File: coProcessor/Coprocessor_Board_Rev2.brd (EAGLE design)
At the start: 101.6 x 101.6 mm, 85 parts, among them IC1 STM32F405RGT6, J1 USB_MINI-B_SMT, J4 30320-6002HB, J5 5008730806, P1 39-30-08?, Q1 L78M05CV, U1 MCP2561-E/P

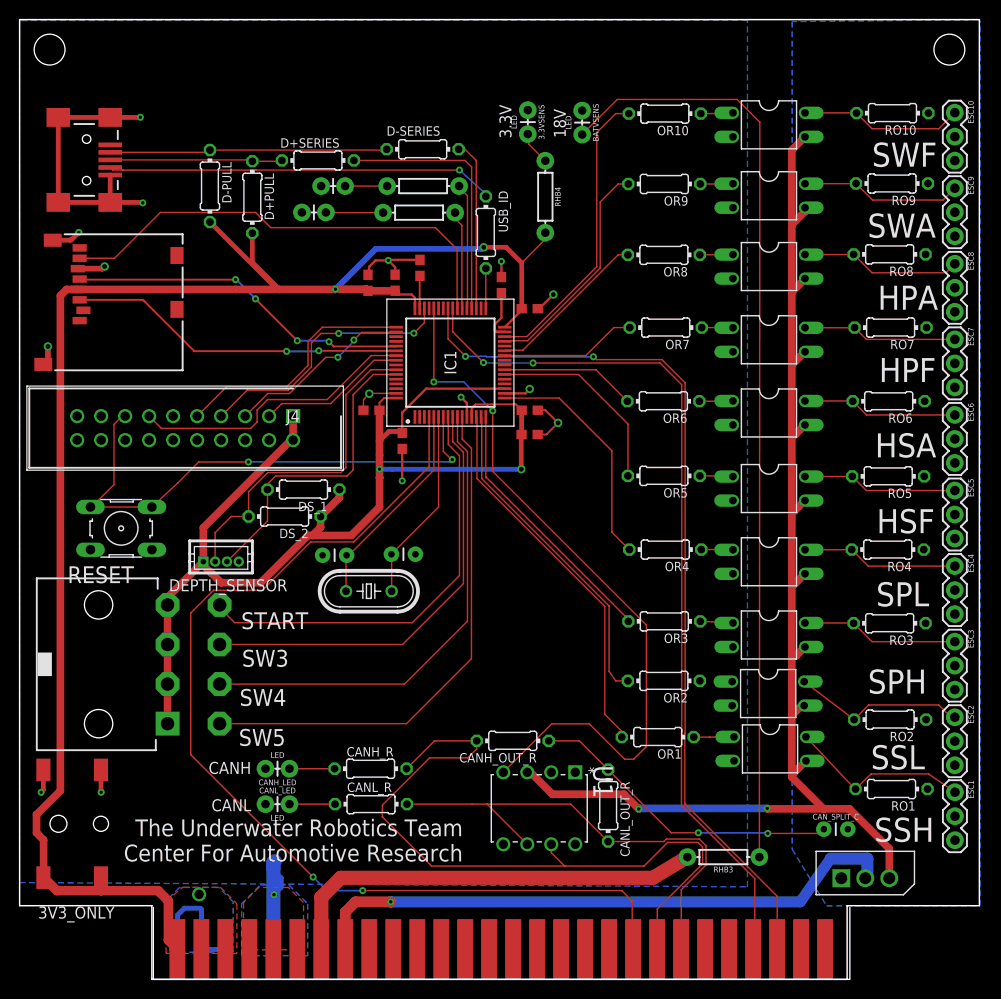
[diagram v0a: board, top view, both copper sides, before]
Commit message: replaced 5v can tran with correct 3.3v
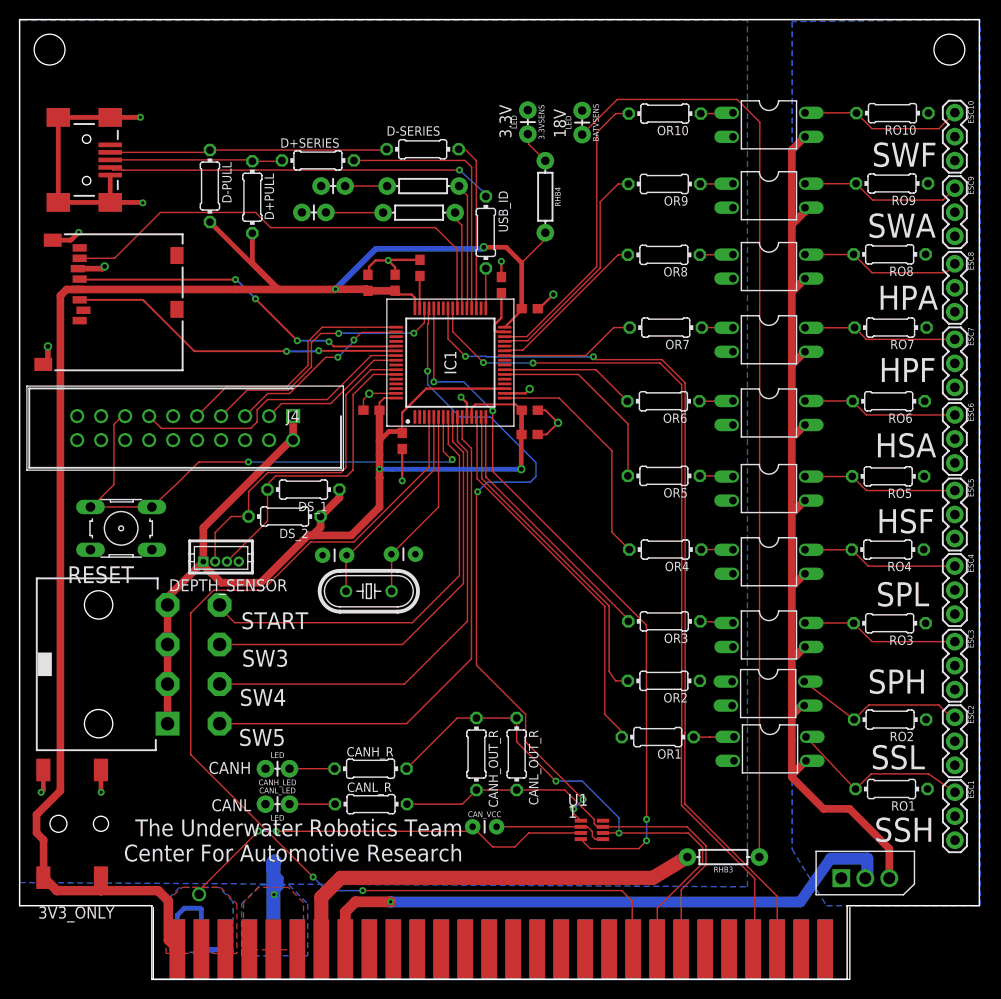
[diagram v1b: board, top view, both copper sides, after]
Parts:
- removed CAN_SPLIT_C: 4700 pF, SparkFun-Capacitors:CAP-PTH-2.54
- added CAN_VCC: .1 uF, SparkFun-Capacitors:CAP-PTH-2.54
- CANH_OUT_R, CANL_OUT_R: value 60 -> 120
- U1: value MCP2561-E/P -> MAX3051ESA; device Microchip-MCP2561-E_P:DIP254P762X533-8 -> MAX3051ESA:8-SOICN
- moved CANL_OUT_R 11.1 mm to (52.6, 23.9)
- moved U1 9.50 mm to (60.6, 15.8), turned to 0 degrees
- moved CANH_OUT_R 4.09 mm to (48.4, 23.9), turned to 270 degrees
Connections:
- removed net SPLIT: CANH_OUT_R.1, CANL_OUT_R.1, CAN_SPLIT_C.1
- removed net VSS: U1.2
- net 3.3V: now also CAN_VCC.1, U1.3
- net 5V: no longer U1.3
- net CAN1_TXD: now also U1.1
- net CANH: now also CANH_OUT_R.1, CANL_OUT_R.1; no longer CANH_OUT_R.2
- net CANL: now also CANH_OUT_R.2
- net GND: now also CANH_LED.P$2, CANL_LED.P$1, CAN_VCC.2, U1.2, U1.8
- net GNDBAT: no longer CANH_LED.P$2, CANL_LED.P$1, CAN_SPLIT_C.2
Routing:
- net CAN1_TXD: track 0.00 -> 71.6 mm, vias 0 -> 4
- net 3.3V: track 314.2 -> 359.4 mm, vias 5 -> 7
- net SPLIT: track 33.4 -> 0.00 mm, vias 2 -> 0
- net 5V: track 135.5 -> 102.5 mm, vias 2 -> 0
- net CANH: track 76.3 -> 56.1 mm, vias 0 -> 2
- net GND: track 88.7 -> 100.8 mm
- net CANL: track 51.8 -> 47.0 mm
- net CAN1_RXD: track 77.0 -> 75.3 mm, vias 2 -> 4

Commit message: 2 pin connector for can. please check... USB moved No usb id line Different switch connector, custom-made 12 pin package Esc names horizontal LEDs for programming Pushbutton for programming 4 leds , 1 pushbutton
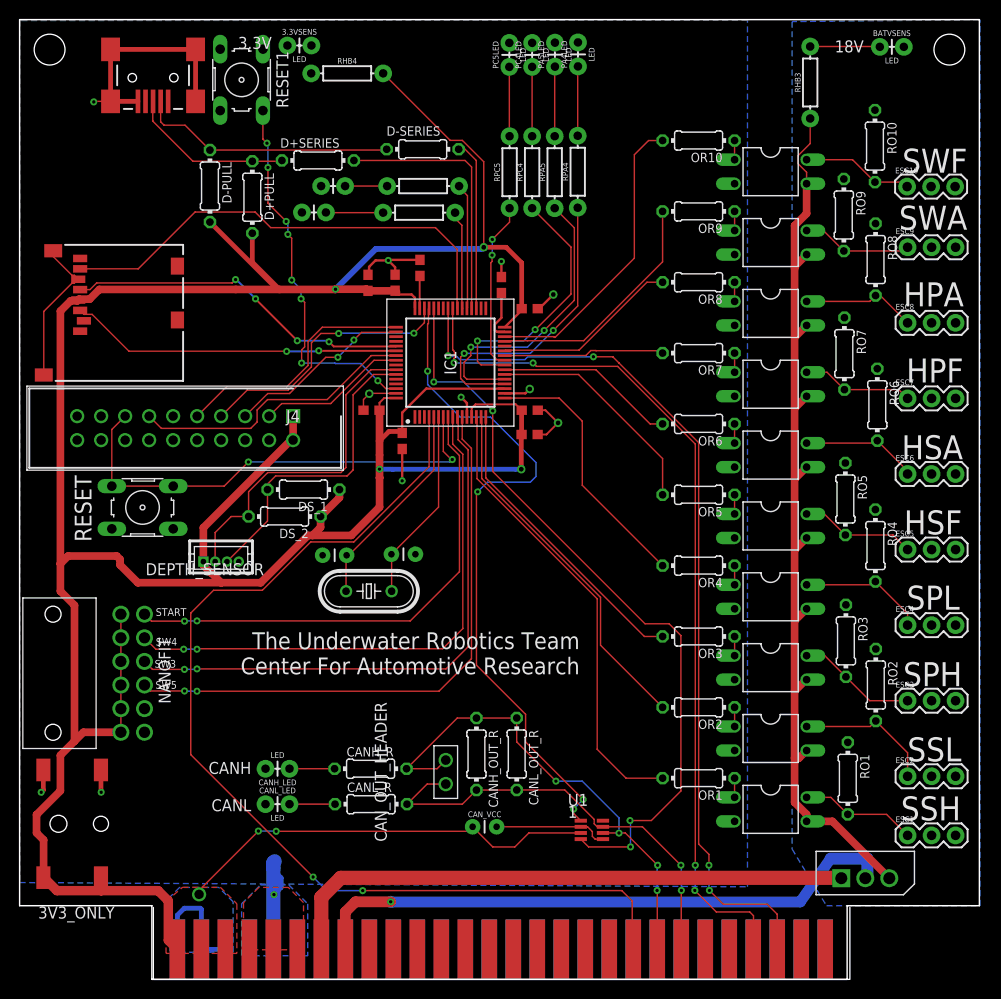
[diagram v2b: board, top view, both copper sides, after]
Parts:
- removed P1: 39-30-08?, con-molex-mini-fit:39-30-?08?
- removed USB_ID: 0Ω, resistor:0204/7
- added CAN_OUT_HEADER: (no value), Wurth_Elektronik_Electromechanic_Board_to_Board_Connectors_rev16a:61300211821
- added PA4LED, PA5LED, PC4LED, PC5LED: LED, SparkFun-Resistors:AXIAL-0.1
- added RESET1: (no value), switch-omron:B3F-10XX
- added RPA4, RPA5, RPC4, RPC5: 1k, SparkFun-Resistors:AXIAL-0.3
- added U$2: 105314-2112, 105314-2112 nanofit hdr:105314-2112
- RHB3: value 7k -> 1.5k
- moved RHB3 82.5 mm to (83.7, 94.9), turned to 90 degrees
- moved BATVSENS 33.7 mm to (92.3, 98.7), turned to 0 degrees
- moved 3.3VSENS 25.5 mm to (29.6, 98.9), turned to 0 degrees
- moved RHB4 24.7 mm to (34.7, 95.9), turned to 0 degrees
- moved J1 11.2 mm to (14.1, 95.4), turned to 270 degrees
- moved ESC10 9.31 mm to (93.9, 83.9), turned to 0 degrees
- moved ESC2 8.00 mm to (94.0, 21.5), turned to 0 degrees
- moved ESC3 8.00 mm to (94.0, 29.5), turned to 0 degrees
- moved ESC4 8.00 mm to (94.0, 37.5), turned to 0 degrees
- moved ESC5 8.00 mm to (94.0, 45.5), turned to 0 degrees
- moved ESC6 8.00 mm to (94.0, 53.5), turned to 0 degrees
- moved ESC7 8.00 mm to (94.0, 61.5), turned to 0 degrees
- moved ESC8 8.00 mm to (94.0, 69.5), turned to 0 degrees
- moved ESC9 8.00 mm to (94.0, 77.5), turned to 0 degrees
- moved ESC1 6.78 mm to (94.0, 15.2), turned to 0 degrees
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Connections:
- removed net OTG_ID: IC1.33, USB_ID.1
- removed net OTG_ID_CON: J1.ID, USB_ID.2
- new net GNDA: BATVSENS.P$2
- new net HEARTBEAT_3: IC1.20, RPA4.P$1
- new net HEARTBEAT_4: IC1.21, RPA5.P$1
- new net N$10: PC4LED.P$1, RPC4.P$2
- new net N$11: PC5LED.P$1, RPC5.P$2
- new net N$12: IC1.62, RESET1.2
- new net N$7: PA4LED.P$1, RPA4.P$2
- new net N$8: PA5LED.P$1, RPA5.P$2
- new net N$9: RESET1.3, RESET1.4
- new net PC4: IC1.24, RPC4.P$1
- new net PC5: IC1.25, RPC5.P$1
- net 18V: now also Q1.1; no longer RHB3.P$2
- net 3.3V: now also U$2.CK10, U$2.CK11, U$2.CK12, U$2.CK7, U$2.CK8, U$2.CK9; no longer P1.1, P1.2, P1.3, P1.4
- net 5V: now also RHB3.P$1
- net CANH: now also CAN_OUT_HEADER.2
- net CANL: now also CAN_OUT_HEADER.1
- net GND: now also PA4LED.P$2, PA5LED.P$2, PC4LED.P$2, PC5LED.P$2
- net GNDBAT: no longer BATVSENS.P$1, Q1.1
- net MISSION_START: now also U$2.CK6; no longer P1.8
- net N$3: now also BATVSENS.P$1, RHB3.P$2; no longer BATVSENS.P$2, RHB3.P$1
- net SWITCH_3: now also U$2.CK5; no longer P1.7
- net SWITCH_4: now also U$2.CK4; no longer P1.6
- net SWITCH_5: now also U$2.CK3; no longer P1.5
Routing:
- net N$3: track 99.1 -> 7.39 mm
- net OTG_ID_CON: track 41.1 -> 0.00 mm, vias 1 -> 0
- net N$12: track 0.00 -> 39.8 mm, vias 0 -> 8
- net 3.3V: track 359.4 -> 396.9 mm
- net HEARTBEAT_3: track 0.00 -> 32.2 mm, vias 0 -> 2
- net HEARTBEAT_4: track 0.00 -> 31.4 mm, vias 0 -> 2
- net PC4: track 0.00 -> 28.0 mm, vias 0 -> 2
- net PC5: track 0.00 -> 18.0 mm, vias 0 -> 2
- net 18V: track 45.7 -> 61.4 mm
- net SWITCH_3: track 46.6 -> 57.9 mm, vias 0 -> 2
- net SWITCH_4: track 51.0 -> 60.4 mm, vias 0 -> 2
- net SURGESTBDHI: track 40.3 -> 48.7 mm
- net N$8: track 0.00 -> 7.38 mm
- net N$7: track 0.00 -> 7.35 mm
- net N$11: track 0.00 -> 7.35 mm
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
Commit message: added gpio pin connector, erc, fixed some air wires
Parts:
- removed CAN_OUT_HEADER: (no value), Wurth_Elektronik_Electromechanic_Board_to_Board_Connectors_rev16a:61300211821
- added GPIO: (no value), SparkFun-Connectors:1X03
- added J2: (no value), SparkFun-Connectors:1X02
- renumbered RESET1 to DEBUG
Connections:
- removed net N$2: 3.3VSENS.P$1
- new net PB8: GPIO.3, IC1.61
- new net PC13: GPIO.2, IC1.2
- new net PC14: GPIO.1, IC1.3
- net CANH: now also J2.2; no longer CAN_OUT_HEADER.2
- net CANL: now also J2.1; no longer CAN_OUT_HEADER.1
- net GND: now also 3.3VSENS.P$1
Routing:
- net PC13: track 0.00 -> 45.7 mm, vias 0 -> 4
- net PC14: track 0.00 -> 41.8 mm, vias 0 -> 6
- net PB8: track 0.00 -> 38.9 mm, vias 0 -> 4
- net N$9: track 0.00 -> 6.50 mm
- net N$4: track 0.00 -> 2.96 mm
- net GND: track 103.9 -> 106.2 mm, vias 12 -> 13
- net SDIO_DO: track 50.3 -> 51.4 mm
